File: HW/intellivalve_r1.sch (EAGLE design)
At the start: 29 parts, among them IC1 24AA02E484, U4 PIC16F1718-I_SO, U5 XR3085XID, U6 TLC59281DBQ

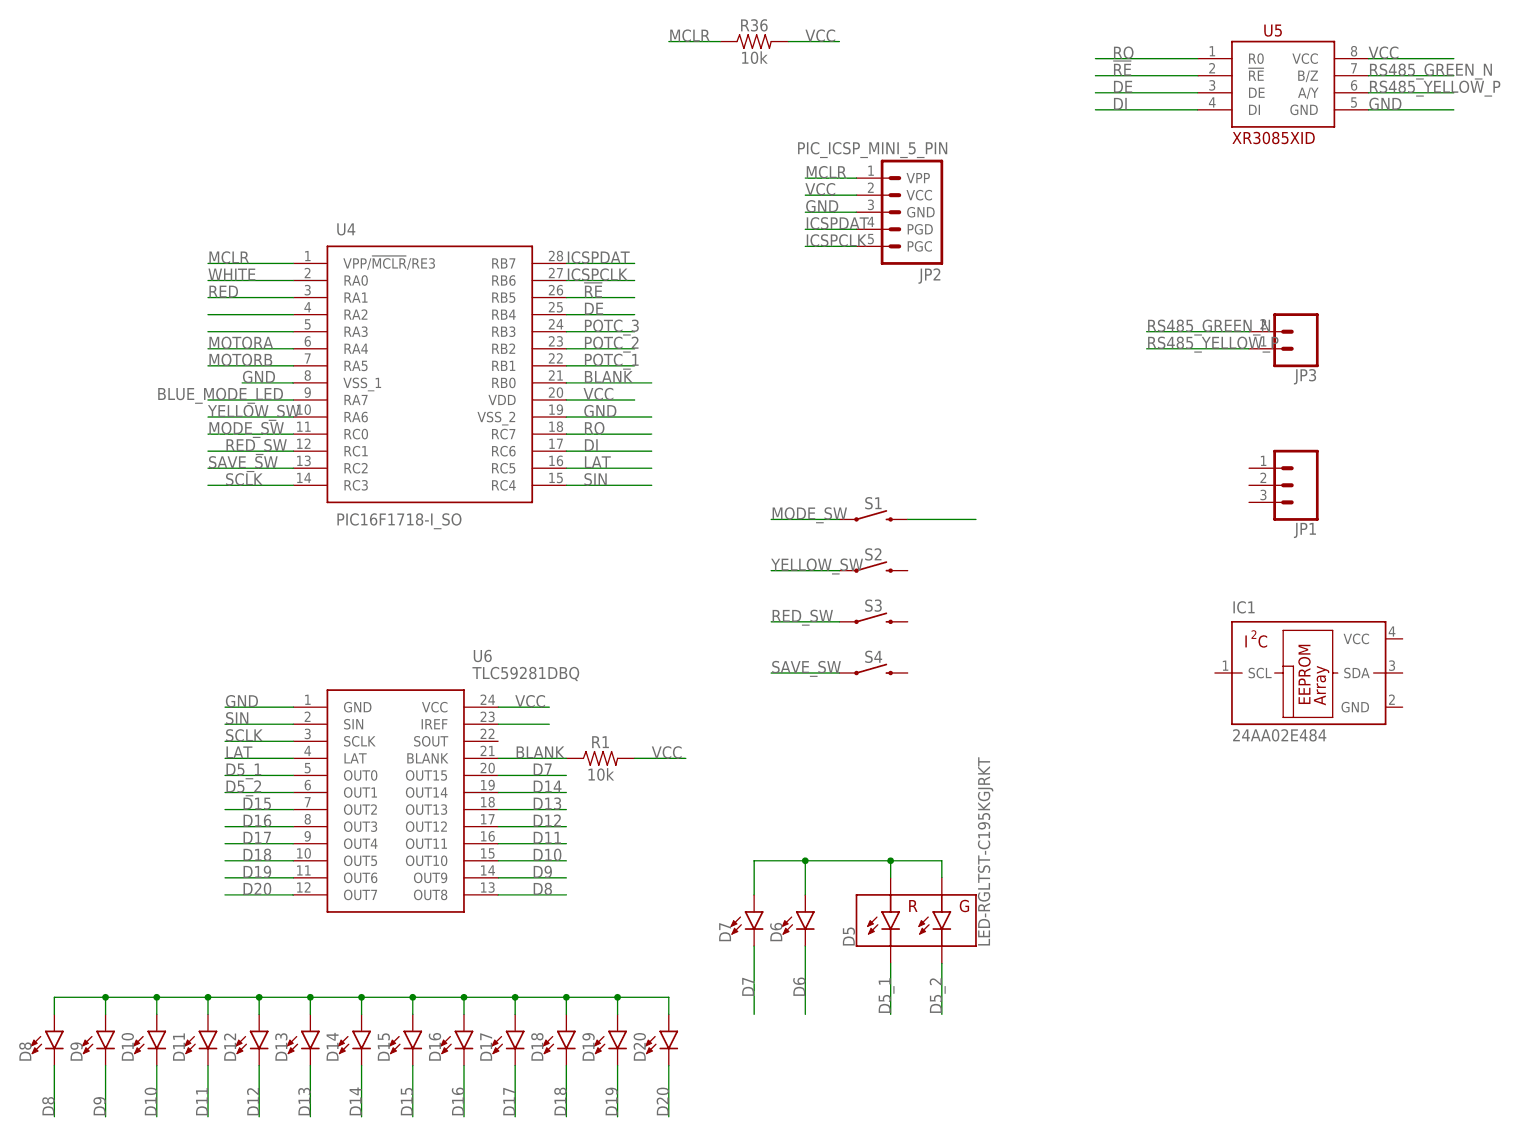
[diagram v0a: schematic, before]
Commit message: latest sync of FW fixes bouncing
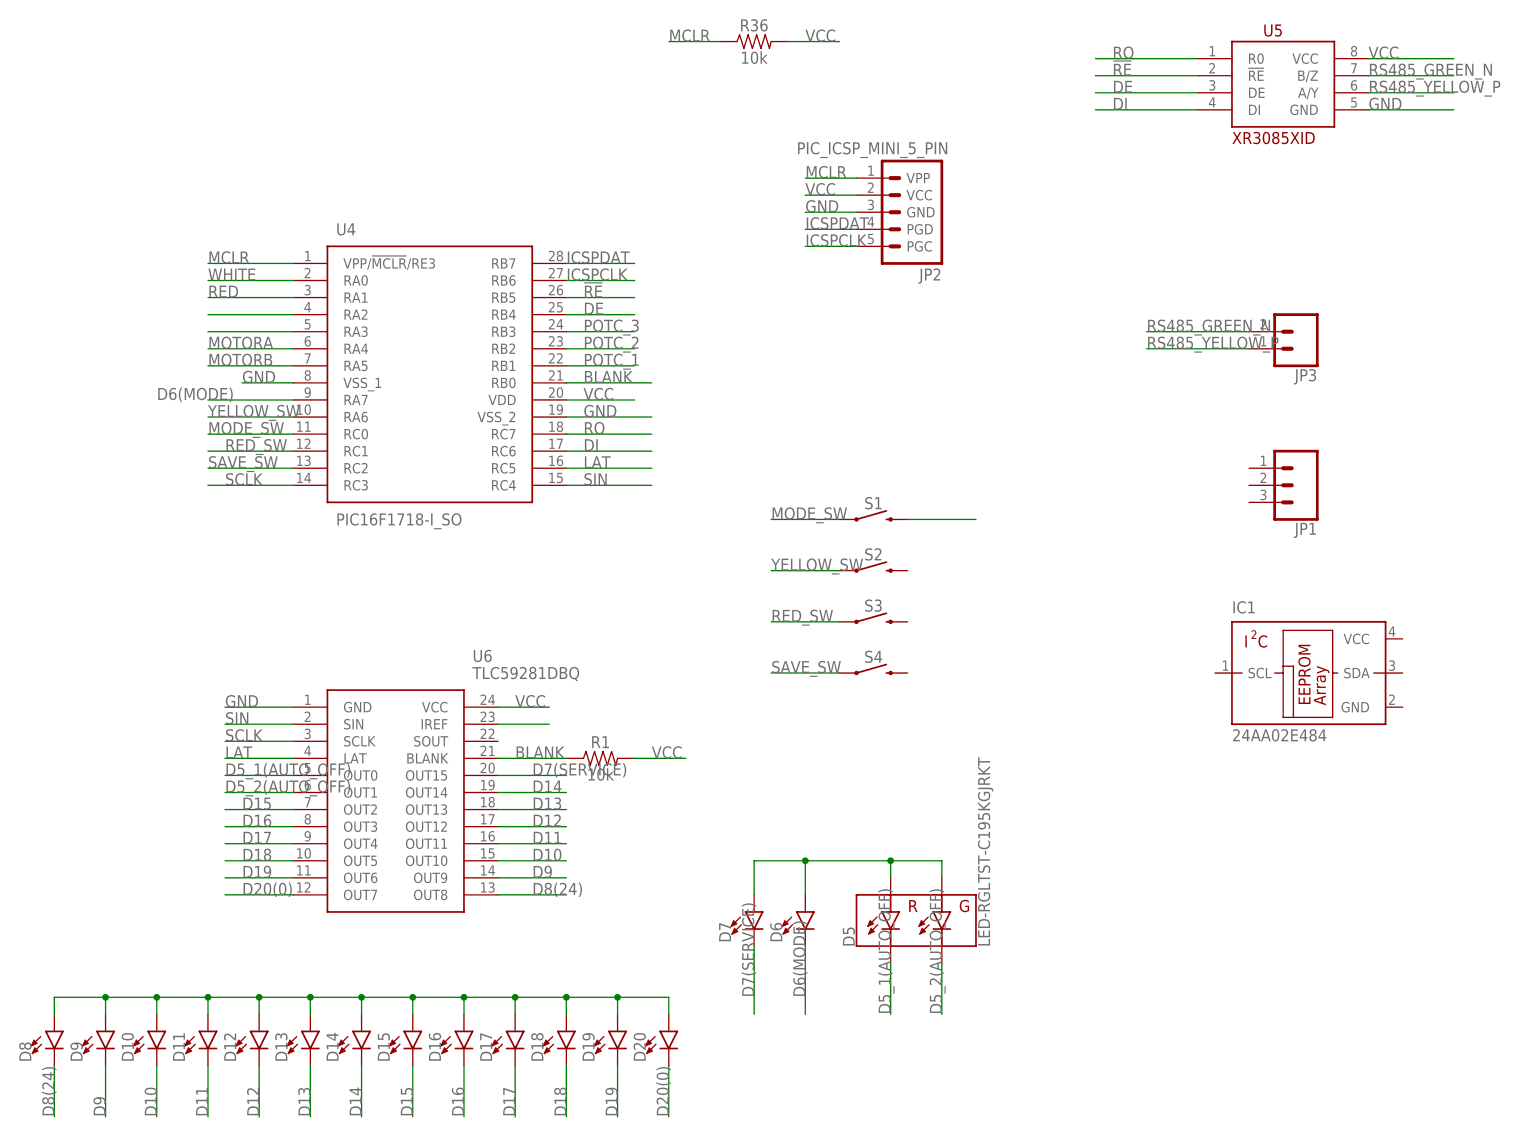
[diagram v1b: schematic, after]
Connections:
- net D20 renamed D20(0)
- net D5_1 renamed D5_1(AUTO_OFF)
- net D5_2 renamed D5_2(AUTO_OFF)
- net D7 renamed D7(SERVICE)
- net D8 renamed D8(24)
- removed net BLUE_MODE_LED: U4.RA7
- removed net D6: D6.C
- new net D6(MODE): D6.C, U4.RA7
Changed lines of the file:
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@@
 </segment>
 </net>
-<net name="D8" class="0">
+<net name="D8(24)" class="0">
 <segment>
 <pinref part="D8" gate="G$1" pin="C"/>
@@
 </segment>
 </net>
-<net name="D20" class="0">
+<net name="D20(0)" class="0">
 <segment>
 <pinref part="D20" gate="G$1" pin="C"/>
@@
 </segment>
 </net>
-<net name="D5_1" class="0">
+<net name="D5_1(AUTO_OFF)" class="0">
 <segment>
 <pinref part="D5" gate="G$1" pin="RC"/>
@@
 </segment>
 </net>
-<net name="D5_2" class="0">
+<net name="D5_2(AUTO_OFF)" class="0">
 <segment>
 <pinref part="D5" gate="G$1" pin="GC"/>
@@
 </segment>
 </net>
-<net name="D7" class="0">
+<net name="D7(SERVICE)" class="0">
 <segment>
 <pinref part="D7" gate="G$1" pin="C"/>
@@
 </segment>
 </net>
-<net name="D6" class="0">
+<net name="D6(MODE)" class="0">
 <segment>
 <pinref part="D6" gate="G$1" pin="C"/>
 <wire x1="149.86" y1="35.56" x2="149.86" y2="25.4" width="0.1524" layer="91"/>
 <label x="149.86" y="27.94" size="1.778" layer="95" rot="R90"/>
+</segment>
+<segment>
+<pinref part="U4" gate="G$1" pin="RA7"/>
+<wire x1="73.66" y1="116.84" x2="60.96" y2="116.84" width="0.1524" layer="91"/>
+<label x="53.34" y="116.84" size="1.778" layer="95"/>
 </segment>
 </net>
@@
 </segment>
 </net>
-<net name="BLUE_MODE_LED" class="0">
-<segment>
-<pinref part="U4" gate="G$1" pin="RA7"/>
-<wire x1="73.66" y1="116.84" x2="60.96" y2="116.84" width="0.1524" layer="91"/>
-<label x="53.34" y="116.84" size="1.778" layer="95"/>
-</segment>
-</net>
